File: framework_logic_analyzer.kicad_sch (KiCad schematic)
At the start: 76 parts, among them IC1 TXU0104QWBQARQ1, IC2 TXU0104QWBQARQ1, IC3 TXU0104QWBQARQ1, IC4 TXU0104QWBQARQ1, IC5 CYUSB3014-BZXC, J1 Conn_02x08_Odd_Even, J2 Conn_02x08_Odd_Even, J3 Conn_ARM_JTAG_SWD_10, Q1 MMBT3904, Q2 MMBT3904, Q3 MMBT3904, U5 M24M02-DR, Y1 19.200 MHz

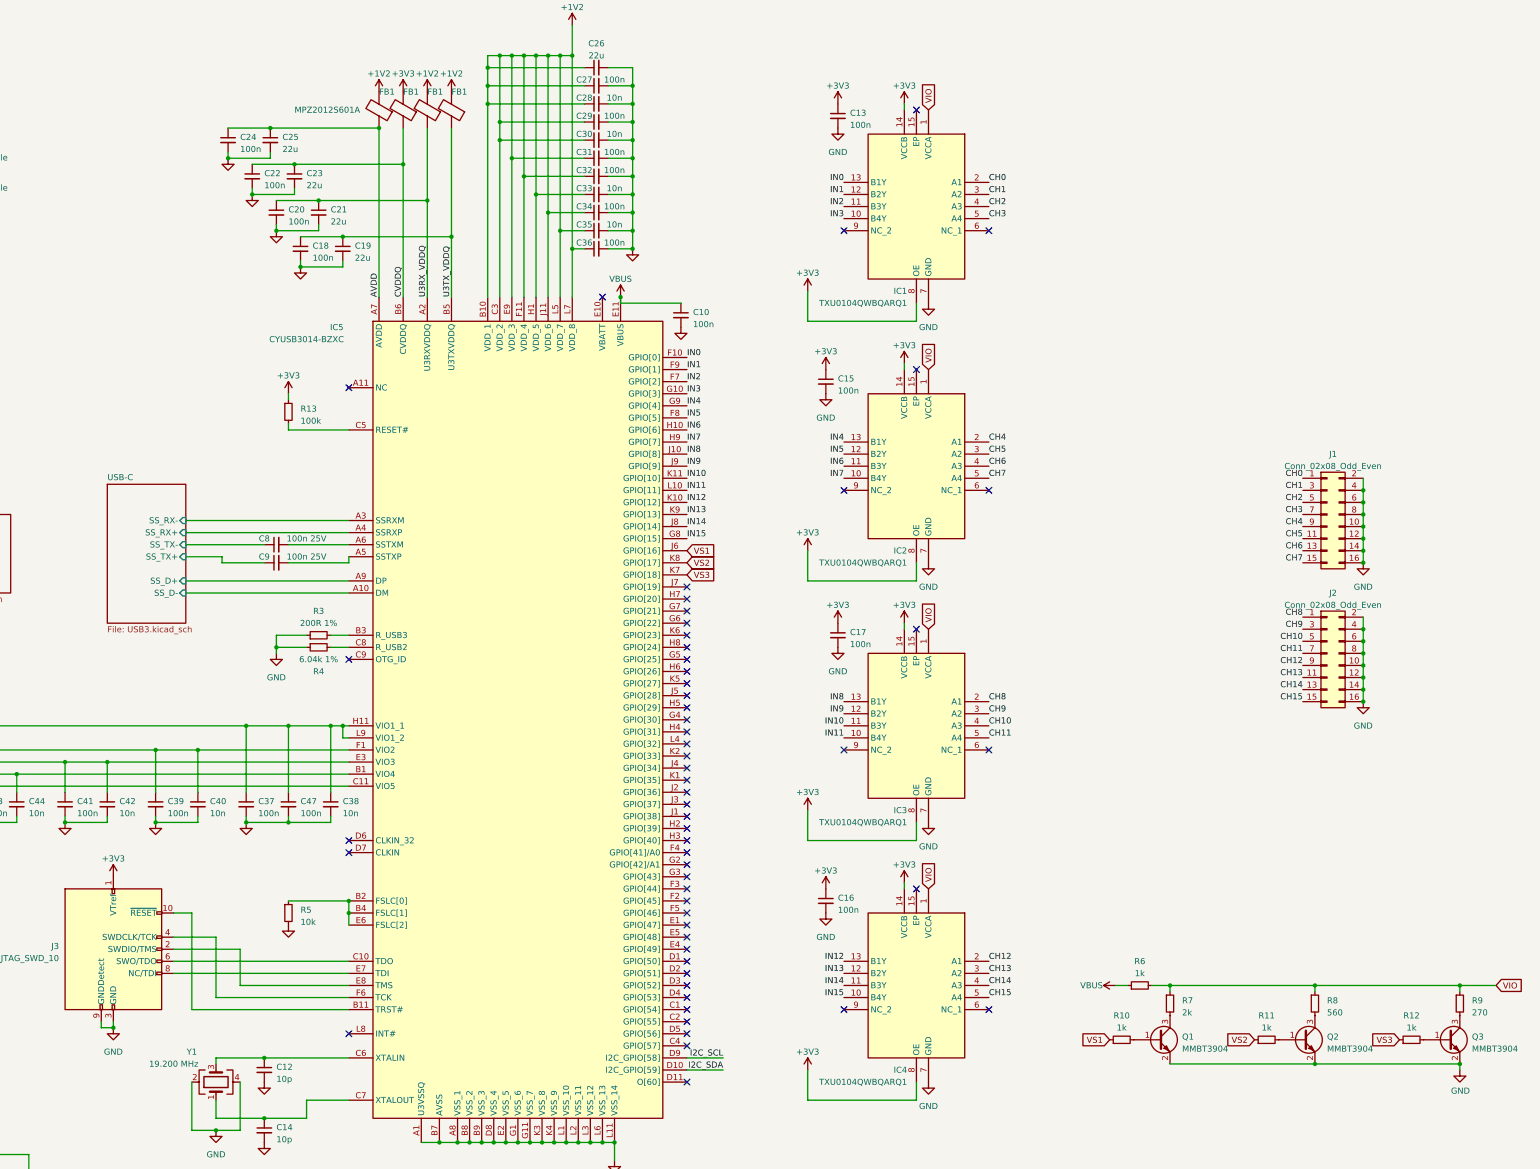
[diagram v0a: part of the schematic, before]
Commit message: update to kicad 9
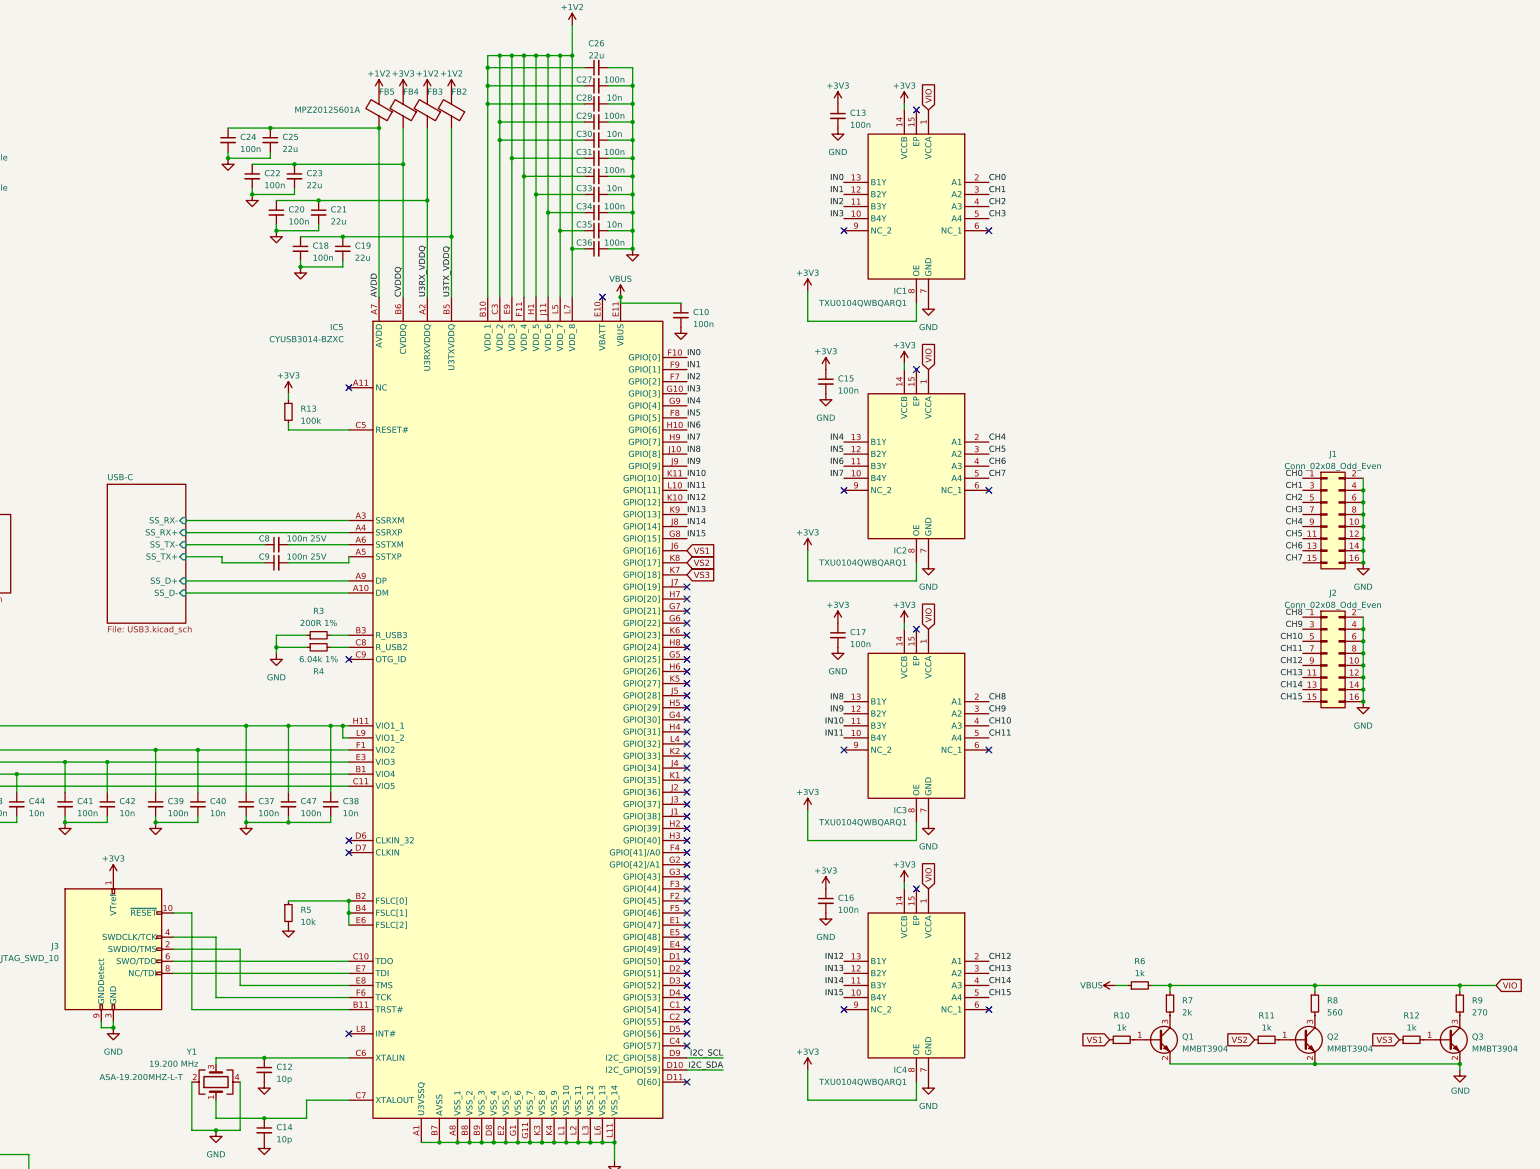
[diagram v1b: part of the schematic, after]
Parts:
- Y1: mpn (none) -> ASA-19.200MHZ-L-T
- renumbered FB1 to FB2, FB1 to FB3, FB1 to FB4, FB1 to FB5

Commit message: begin big refactor
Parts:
- removed C13, C15, C16, C17: 100n, Capacitor_SMD:C_0402_1005Metric, symbol Device:C_Small
- removed IC1, IC2, IC3, IC4: TXU0104QWBQARQ1, TXU0104:TXU0104QWBQARQ1, symbol TXU0104QWBQARQ1:TXU0104QWBQARQ1
- removed J1, J2: Conn_02x08_Odd_Even, 20021311-00016T4LF:20021311-00016T4LF, symbol Connector_Generic:Conn_02x08_Odd_Even
- removed TP2, TP3, TP4: TestPoint, TestPoint:TestPoint_Pad_1.5x1.5mm, symbol Connector:TestPoint
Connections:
- no-connect marks 62 -> 50
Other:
- added sheet Signal Input (signal_input.kicad_sch)
- note added: "I2C EEPROM"
- note added: "Mechanical"
- note added: "voltage selector"
- moved on the sheet: C10, C12, C14, C18, C19, C20, C21, C22, C23, C24, C25, C26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

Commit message: further routing
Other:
- moved on the sheet: C8, C9
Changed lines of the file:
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@@
 	(wire
 		(pts
-			(xy 86.36 118.11) (xy 102.87 118.11)
+			(xy 86.36 118.11) (xy 106.68 118.11)
 		)
 		(stroke
@@
 	(wire
 		(pts
-			(xy 107.95 118.11) (xy 120.65 118.11)
+			(xy 111.76 118.11) (xy 120.65 118.11)
 		)
 		(stroke
@@
 	(wire
 		(pts
-			(xy 102.87 121.92) (xy 93.98 121.92)
-		)
-		(stroke
-			(width 0)
-			(type default)
-		)
-	)
-	(wire
-		(pts
 			(xy 252.73 31.75) (xy 252.73 33.02)
 		)
@@
 	(wire
 		(pts
-			(xy 93.98 120.65) (xy 86.36 120.65)
-		)
-		(stroke
-			(width 0)
-			(type default)
-		)
-	)
-	(wire
-		(pts
 			(xy 127 30.48) (xy 127 66.04)
 		)
@@
 	(wire
 		(pts
-			(xy 120.65 121.92) (xy 107.95 121.92)
+			(xy 120.65 120.65) (xy 99.06 120.65)
 		)
 		(stroke
@@
 	(wire
 		(pts
-			(xy 120.65 120.65) (xy 120.65 121.92)
-		)
-		(stroke
-			(width 0)
-			(type default)
-		)
-	)
-	(wire
-		(pts
 			(xy 251.46 195.58) (xy 255.27 195.58)
 		)
@@
 	(wire
 		(pts
-			(xy 31.75 176.53) (xy 22.86 176.53)
+			(xy 93.98 120.65) (xy 86.36 120.65)
 		)
 		(stroke
@@
 	(wire
 		(pts
-			(xy 86.36 113.03) (xy 120.65 113.03)
+			(xy 31.75 176.53) (xy 22.86 176.53)
 		)
 		(stroke
@@
 	(wire
 		(pts
-			(xy 68.58 218.44) (xy 68.58 219.71)
+			(xy 86.36 113.03) (xy 120.65 113.03)
 		)
 		(stroke
@@
 	(wire
 		(pts
-			(xy 93.98 121.92) (xy 93.98 120.65)
+			(xy 68.58 218.44) (xy 68.58 219.71)
 		)
 		(stroke
@@
 	(symbol
 		(lib_id "Device:C_Small")
-		(at 105.41 118.11 90)
+		(at 109.22 118.11 90)
 		(unit 1)
 		(exclude_from_sim no)
@@
 		(dnp no)
 		(property "Reference" "C8"
-			(at 102.87 116.84 90)
+			(at 106.68 116.84 90)
 			(effects
 				(font
@@
 		)
 		(property "Value" "100n 25V"
-			(at 111.76 116.84 90)
+			(at 115.57 116.84 90)
 			(effects
 				(font
@@
 		)
 		(property "Footprint" "Capacitor_SMD:C_0402_1005Metric"
-			(at 105.41 118.11 0)
+			(at 109.22 118.11 0)
 			(effects
 				(font
@@
 		)
 		(property "Datasheet" "~"
-			(at 105.41 118.11 0)
+			(at 109.22 118.11 0)
 			(effects
 				(font
@@
 		)
 		(property "Description" ""
-			(at 105.41 118.11 0)
+			(at 109.22 118.11 0)
 			(effects
 				(font
@@
 	(symbol
 		(lib_id "Device:C_Small")
-		(at 105.41 121.92 90)
+		(at 96.52 120.65 90)
 		(unit 1)
 		(exclude_from_sim no)
@@
 		(dnp no)
 		(property "Reference" "C9"
-			(at 102.87 120.65 90)
+			(at 93.98 119.38 90)
 			(effects
 				(font
@@
 		)
 		(property "Value" "100n 25V"
-			(at 111.76 120.65 90)
+			(at 102.87 119.38 90)
 			(effects
 				(font
@@
 		)
 		(property "Footprint" "Capacitor_SMD:C_0402_1005Metric"
-			(at 105.41 121.92 0)
+			(at 96.52 120.65 0)
 			(effects
 				(font
@@
 		)
 		(property "Datasheet" "~"
-			(at 105.41 121.92 0)
+			(at 96.52 120.65 0)
 			(effects
 				(font
@@
 		)
 		(property "Description" ""
-			(at 105.41 121.92 0)
+			(at 96.52 120.65 0)
 			(effects
 				(font

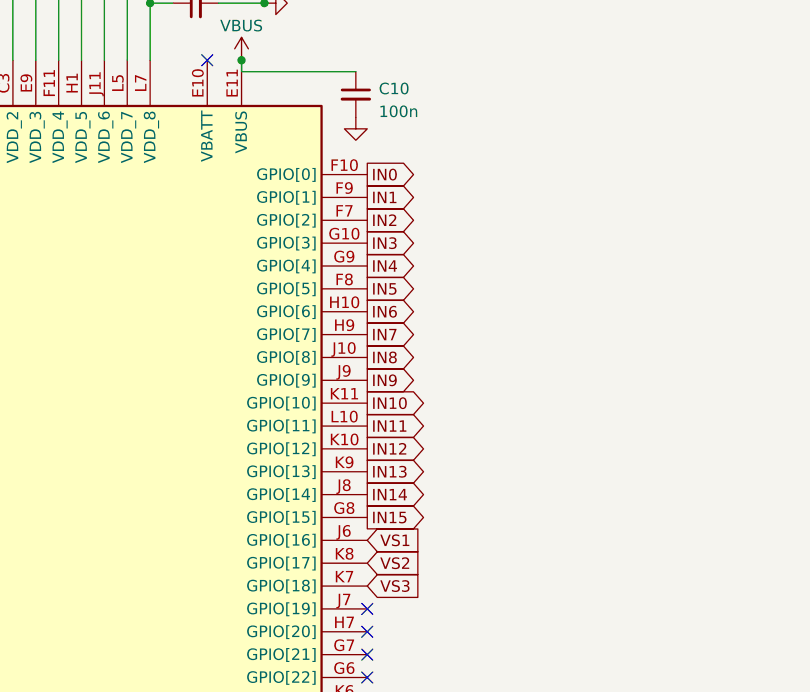
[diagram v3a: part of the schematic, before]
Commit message: more routing, add differential pair netclass
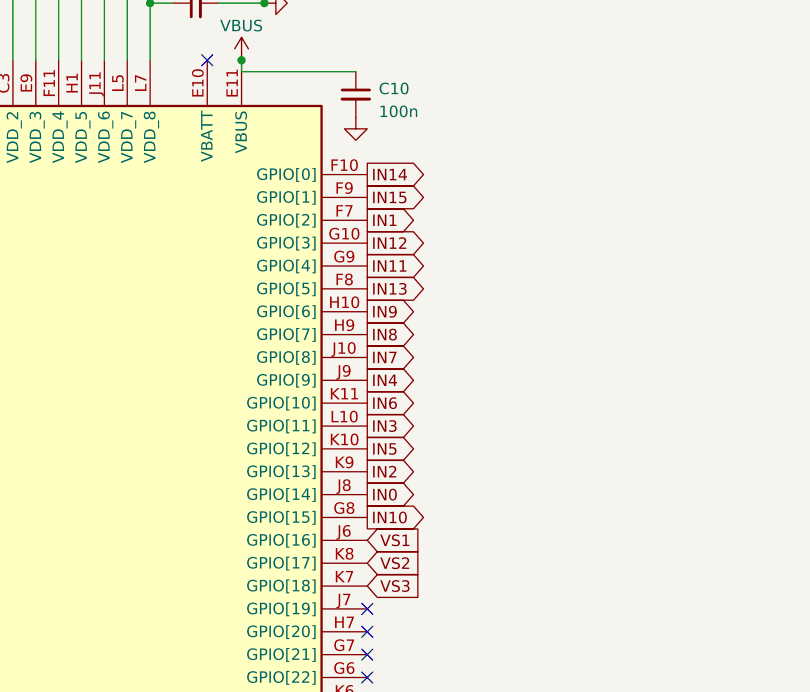
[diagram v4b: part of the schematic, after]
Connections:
- net IN0: now also IC5.J8 (GPIO[14]); no longer IC5.F10 (GPIO[0])
- net IN1: now also IC5.F7 (GPIO[2]); no longer IC5.F9 (GPIO[1])
- net IN10: now also IC5.G8 (GPIO[15]); no longer IC5.K11 (GPIO[10])
- net IN11: now also IC5.G9 (GPIO[4]); no longer IC5.L10 (GPIO[11])
- net IN12: now also IC5.G10 (GPIO[3]); no longer IC5.K10 (GPIO[12])
- net IN13: now also IC5.F8 (GPIO[5]); no longer IC5.K9 (GPIO[13])
- net IN14: now also IC5.F10 (GPIO[0]); no longer IC5.J8 (GPIO[14])
- net IN15: now also IC5.F9 (GPIO[1]); no longer IC5.G8 (GPIO[15])
- net IN2: now also IC5.K9 (GPIO[13]); no longer IC5.F7 (GPIO[2])
- net IN3: now also IC5.L10 (GPIO[11]); no longer IC5.G10 (GPIO[3])
- net IN4: now also IC5.J9 (GPIO[9]); no longer IC5.G9 (GPIO[4])
- net IN5: now also IC5.K10 (GPIO[12]); no longer IC5.F8 (GPIO[5])
- net IN6: now also IC5.K11 (GPIO[10]); no longer IC5.H10 (GPIO[6])
- net IN7: now also IC5.J10 (GPIO[8]); no longer IC5.H9 (GPIO[7])
- net IN8: now also IC5.H9 (GPIO[7]); no longer IC5.J10 (GPIO[8])
- net IN9: now also IC5.H10 (GPIO[6]); no longer IC5.J9 (GPIO[9])

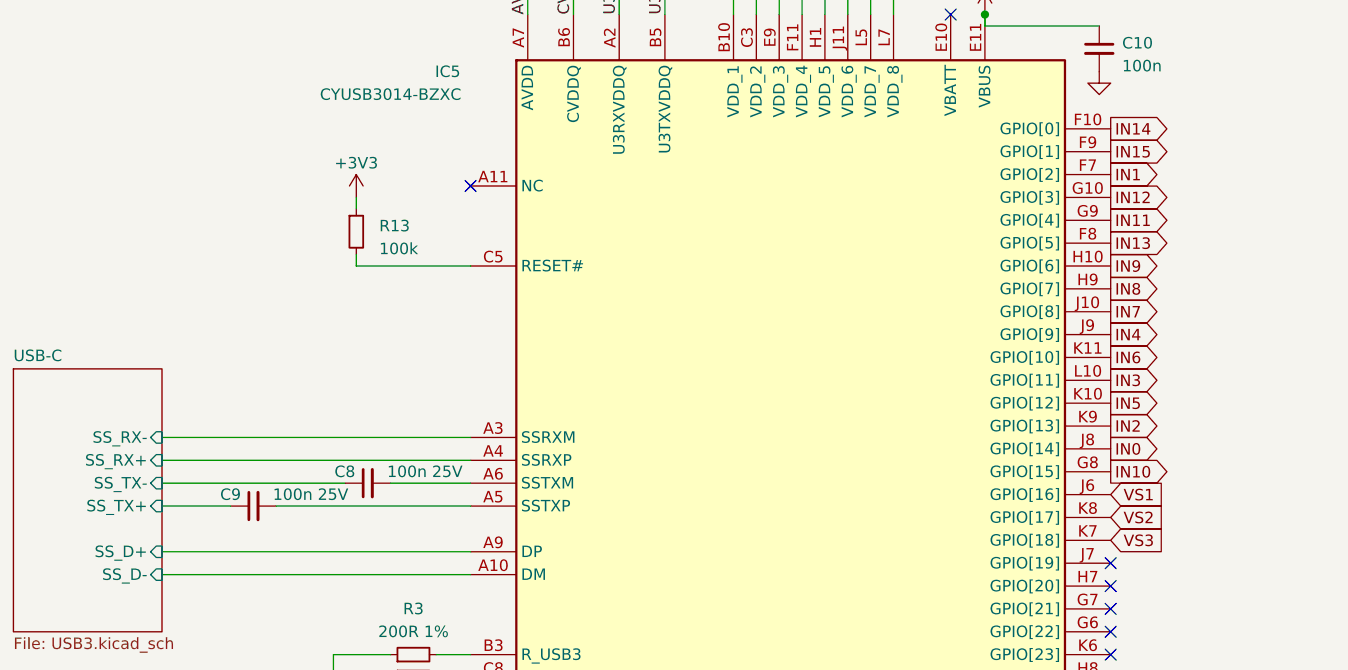
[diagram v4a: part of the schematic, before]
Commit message: length match input channels
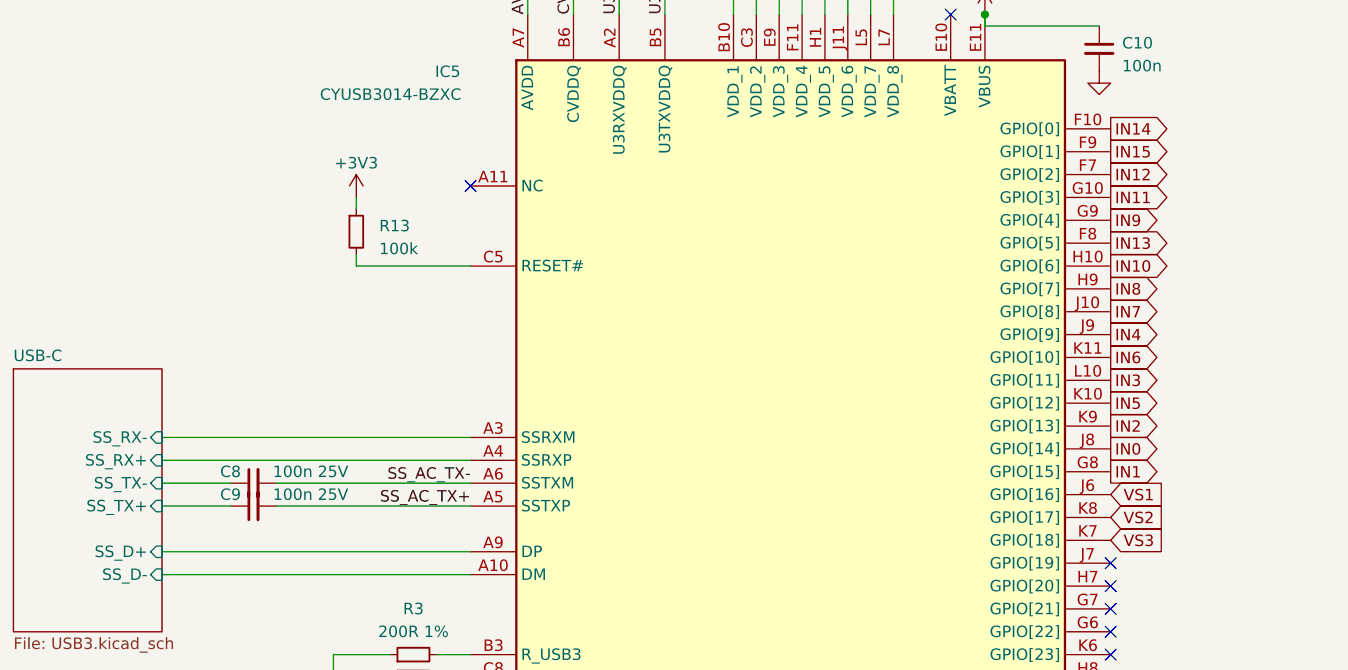
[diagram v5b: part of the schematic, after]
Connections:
- net IN1: now also IC5.G8 (GPIO[15]); no longer IC5.F7 (GPIO[2])
- net IN10: now also IC5.H10 (GPIO[6]); no longer IC5.G8 (GPIO[15])
- net IN11: now also IC5.G10 (GPIO[3]); no longer IC5.G9 (GPIO[4])
- net IN12: now also IC5.F7 (GPIO[2]); no longer IC5.G10 (GPIO[3])
- net IN9: now also IC5.G9 (GPIO[4]); no longer IC5.H10 (GPIO[6])
- net SS_AC_TX+: now reaches C9.2, IC5.A5 (SSTXP)
- net SS_AC_TX-: now reaches C8.2, IC5.A6 (SSTXM)
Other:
- moved on the sheet: C8
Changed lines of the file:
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@@
 	(wire
 		(pts
-			(xy 86.36 118.11) (xy 106.68 118.11)
+			(xy 86.36 118.11) (xy 93.98 118.11)
 		)
 		(stroke
@@
 	(wire
 		(pts
-			(xy 111.76 118.11) (xy 120.65 118.11)
+			(xy 99.06 118.11) (xy 120.65 118.11)
 		)
 		(stroke
@@
 		)
 	)
+	(label "SS_AC_TX-"
+		(at 120.65 118.11 180)
+		(effects
+			(font
+				(size 1.27 1.27)
+			)
+			(justify right bottom)
+		)
+	)
 	(label "U3RX_VDDQ"
 		(at 137.16 66.04 90)
@@
 		)
 	)
+	(label "SS_AC_TX+"
+		(at 120.65 120.65 180)
+		(effects
+			(font
+				(size 1.27 1.27)
+			)
+			(justify right bottom)
+		)
+	)
 	(label "I2C_SDA"
 		(at 234.95 40.64 0)
@@
 	(global_label "IN9"
 		(shape output)
-		(at 191.77 93.98 0)
+		(at 191.77 88.9 0)
 		(fields_autoplaced yes)
 		(effects
@@
 		)
 		(property "Intersheetrefs" "${INTERSHEET_REFS}"
-			(at 197.2458 93.98 0)
+			(at 197.2458 88.9 0)
 			(effects
 				(font
@@
 	(global_label "IN11"
 		(shape output)
-		(at 191.77 88.9 0)
+		(at 191.77 86.36 0)
 		(fields_autoplaced yes)
 		(effects
@@
 		)
 		(property "Intersheetrefs" "${INTERSHEET_REFS}"
-			(at 197.2458 88.9 0)
+			(at 197.2458 86.36 0)
 			(effects
 				(font
@@
 	(global_label "IN1"
 		(shape output)
-		(at 191.77 83.82 0)
+		(at 191.77 116.84 0)
 		(fields_autoplaced yes)
 		(effects
@@
 		)
 		(property "Intersheetrefs" "${INTERSHEET_REFS}"
-			(at 197.2458 83.82 0)
+			(at 197.2458 116.84 0)
 			(effects
 				(font
@@
 	(global_label "IN12"
 		(shape output)
-		(at 191.77 86.36 0)
+		(at 191.77 83.82 0)
 		(fields_autoplaced yes)
 		(effects
@@
 		)
 		(property "Intersheetrefs" "${INTERSHEET_REFS}"
-			(at 197.2458 86.36 0)
+			(at 197.2458 83.82 0)
 			(effects
 				(font
@@
 	(global_label "IN10"
 		(shape output)
-		(at 191.77 116.84 0)
+		(at 191.77 93.98 0)
 		(fields_autoplaced yes)
 		(effects
@@
 		)
 		(property "Intersheetrefs" "${INTERSHEET_REFS}"
-			(at 197.2458 116.84 0)
+			(at 197.2458 93.98 0)
 			(effects
 				(font
@@
 		)
 	)
+	(netclass_flag ""
+		(length 2.54)
+		(shape round)
+		(at 120.65 120.65 180)
+		(fields_autoplaced yes)
+		(effects
+			(font
+				(size 1.27 1.27)
+			)
+			(justify right bottom)
+		)
+		(property "Netclass" "90R"
+			(at 121.2596 123.19 0)
+			(effects
+				(font
+					(size 1.27 1.27)
+				)
+				(justify left)
+			)
+		)
+		(property "Component Class" ""
+			(at -144.78 53.34 0)
+			(effects
+				(font
+					(size 1.27 1.27)
+					(italic yes)
+				)
+			)
+		)
+	)
+	(netclass_flag ""
+		(length 2.54)
+		(shape round)
+		(at 120.65 118.11 180)
+		(fields_autoplaced yes)
+		(effects
+			(font
+				(size 1.27 1.27)
+			)
+			(justify right bottom)
+		)
+		(property "Netclass" "90R"
+			(at 121.2596 120.65 0)
+			(effects
+				(font
+					(size 1.27 1.27)
+				)
+				(justify left)
+			)
+		)
+		(property "Component Class" ""
+			(at -144.78 50.8 0)
+			(effects
+				(font
+					(size 1.27 1.27)
+					(italic yes)
+				)
+			)
+		)
+	)
 	(symbol
 		(lib_id "power:+1V2")
@@
 	(symbol
 		(lib_id "Device:C_Small")
-		(at 109.22 118.11 90)
+		(at 96.52 118.11 90)
 		(unit 1)
 		(exclude_from_sim no)
@@
 		(dnp no)
 		(property "Reference" "C8"
-			(at 106.68 116.84 90)
+			(at 93.98 116.84 90)
 			(effects
 				(font
@@
 		)
 		(property "Value" "100n 25V"
-			(at 115.57 116.84 90)
+			(at 102.87 116.84 90)
 			(effects
 				(font
@@
 		)
 		(property "Footprint" "Capacitor_SMD:C_0402_1005Metric"
-			(at 109.22 118.11 0)
+			(at 96.52 118.11 0)
 			(effects
 				(font
@@
 		)
 		(property "Datasheet" "~"
-			(at 109.22 118.11 0)
+			(at 96.52 118.11 0)
 			(effects
 				(font
@@
 		)
 		(property "Description" ""
-			(at 109.22 118.11 0)
+			(at 96.52 118.11 0)
 			(effects
 				(font
